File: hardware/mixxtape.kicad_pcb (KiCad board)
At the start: 2 copper layers, 99.5 x 63.5 mm, 71 parts, among them J1 USB-C_SMD-TYPE-C-31-M-12_1, J4 TF-SMD_TF-01A, J5 PROG_JIG, SW1 SW-SMD_4P-L5.1-W5.1-P3.70-LS6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, SW2 SW-SMD_4P-L5.1-W5.1-P3.70-LS6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, SW3 SW-SMD_4P-L5.1-W5.1-P3.70-LS6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, SW4 SW-SMD_4P-L5.1-W5.1-P3.70-LS6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, U1 WIFI-SMD_ESP32-WROOM-32E, U2 LGA-8_L4.0-W3.0-R_WMM7040DT0, U3 SOIC-8_L5.3-W5.3-P1.27-LS8.0-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, U4 SOT-223-3_L6.5-W3.4-P2.30-LS7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, U8 SOT-23-5_L3.0-W1.7-P0.95-LS2.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

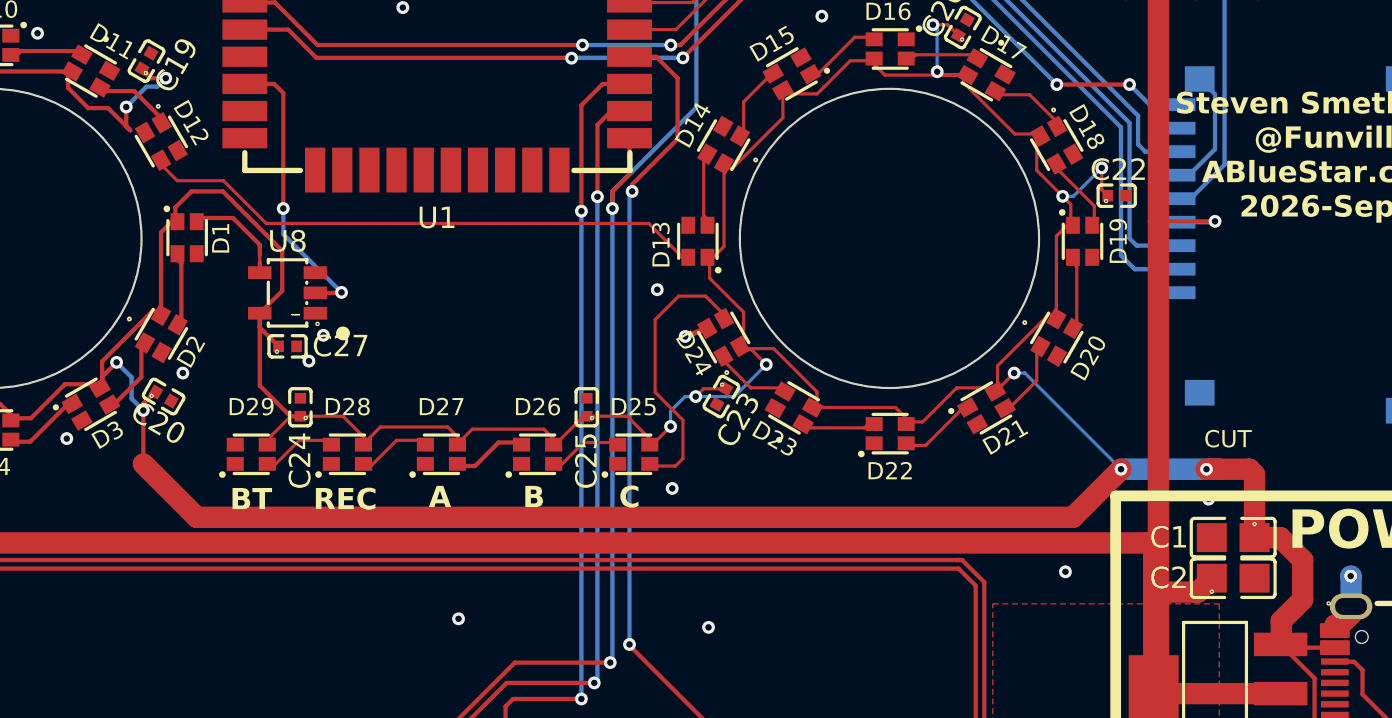
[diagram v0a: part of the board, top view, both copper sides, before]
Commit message: hardware: repair three breaks left by the re-route
The re-route in ee24c0e introduced three faults. DRC found them because the
severities were promoted to error earlier; at the original settings two of the
three would have been warnings.

D12 pad 3 (VBUS) was left 0.693 mm short of its feed - the track stopped
before reaching the pad. D12 would have had no power, and because the LEDs are
a daisy chain that also kills every LED after it. Reconnected on the board's
existing 45-degree house style.

C2's ground was orphaned. The re-route split the F.Cu pour and left an
8.48 mm2 island whose only member was C2 pad 2, with no via to the plane - so
the AMS1117's output capacitor had no ground return and its decoupling did
nothing. Stitched with a GND via at (118.400, 75.350), 1.445 mm clear of the
nearest foreign copper.

A 0.266 mm CC1_SENSE stub was left pointing at nothing. Removed.

Two attempts at that stitching via were rejected before this one, and both
failures are worth recording because they are the same class of mistake: the
first clearance model tested only track ENDPOINTS and put a via 0.067 mm from
a SPI_MISO run; the second approximated pads as circles and put one 0.112 mm
from C2's own 3V3 pad. The version used measures to track segments and to real
pad rectangles.

DRC 0 errors, 0 unconnected. ERC 0/0. Fab package re-exported.

NOT changed by this commit, and worth confirming: the four mounting holes are
byte-identical to before - still 0.350 mm of horizontal skew and 0.250 mm of
vertical. J1 is also unchanged, so the USB-C setback is still 0.767 mm.

Co-Authored-By: Claude Opus 5 <noreply@anthropic.com>
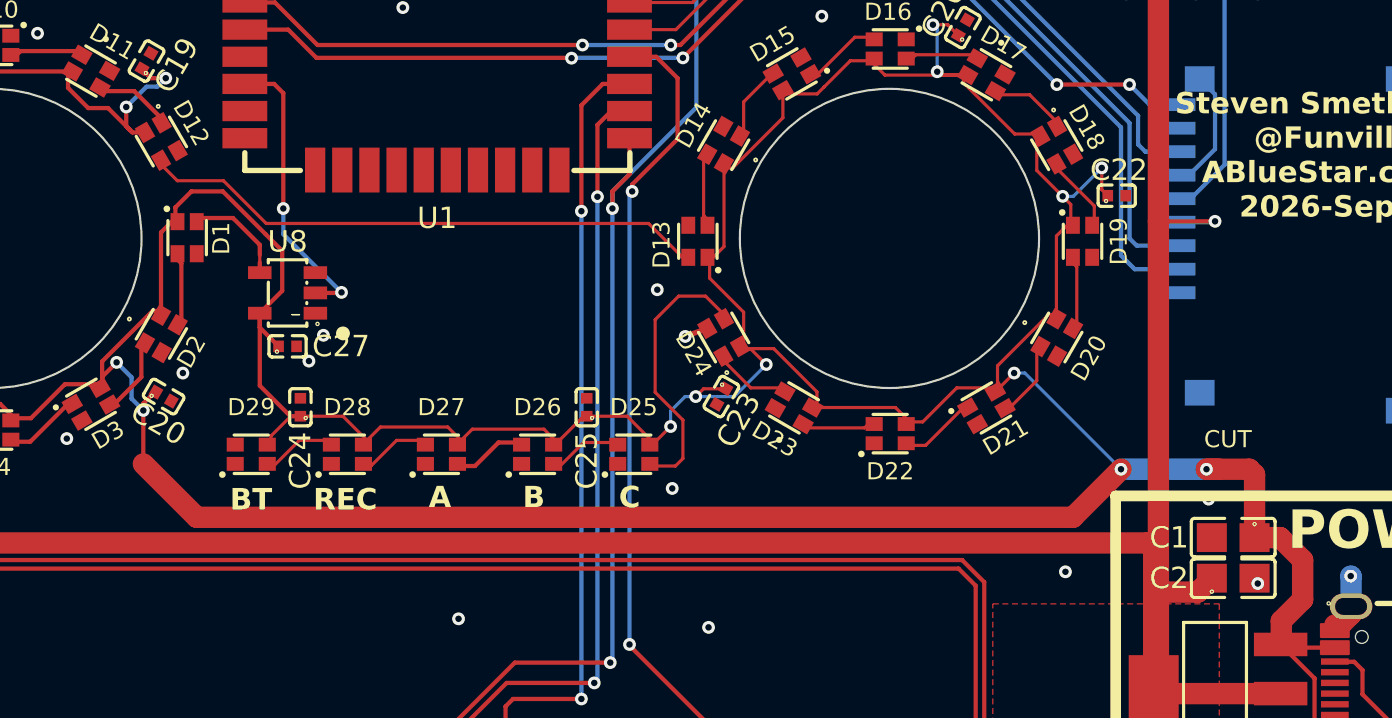
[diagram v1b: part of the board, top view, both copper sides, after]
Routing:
- net VBUS: track 264.7 -> 265.4 mm
- net GND: vias 44 -> 45
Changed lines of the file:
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@@
 	)
 	(via
+		(at 118.4 75.35)
+		(size 0.6)
+		(drill 0.3)
+		(layers "F.Cu" "B.Cu")
+		(tenting
+			(front yes)
+			(back yes)
+		)
+		(net "GND")
+	)
+	(via
 		(at 68.1 65.5)
 		(size 0.6)
@@
 	)
 	(segment
+		(start 65.643 54.143)
+		(end 65.740479 54.24048)
+		(width 0.2)
+		(layer "F.Cu")
+		(net "VBUS")
+	)
+	(segment
 		(start 52.442086 64.186743)
 		(end 53.545141 64.186743)
@@
 	)
 	(segment
+		(start 65.740479 54.24048)
+		(end 66.329517 54.24048)
+		(width 0.2)
+		(layer "F.Cu")
+		(net "VBUS")
+	)
+	(segment
 		(start 99.334786 50.885001)
 		(end 98.109894 52.109894)
@@
 		(width 0.2)
 		(layer "F.Cu")
-		(net "CC1_SENSE")
-	)
-	(segment
-		(start 104.565685 74.25)
-		(end 104.3 74.25)
-		(width 0.2)
-		(layer "F.Cu")
